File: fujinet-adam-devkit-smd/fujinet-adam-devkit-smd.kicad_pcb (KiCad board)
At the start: 2 copper layers, 57.8 x 55.3 mm, 39 parts, among them J1 RJ12, J2 RJ12, J3 SD_Card, Q1 MMBT3904, Q2 MMBT3906, SW1 ButtonA, SW2 ButtonB, SW3 Safe Reset, U1 ESP32-DEVKITC-32U

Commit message: Update docs
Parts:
- U1: value ESP32-DEVKITC-32U -> ESP32-DevKitC-VE

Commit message: Update SMD PCB and Case to v1.1, fix ADAMNet Out port not working
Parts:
- J1: value RJ12 -> In
- J2: value RJ12 -> Out
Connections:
- J2 pad 1: /ADAMNET_DATA -> /ADAMNET_5V
- J2 pad 2: /ADAMNET_RESET -> GND
- J2 pad 5: GND -> /ADAMNET_RESET
- J2 pad 6: /ADAMNET_5V -> /ADAMNET_DATA
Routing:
- net /ADAMNET_5V: track 58.3 -> 68.9 mm
- net /ADAMNET_DATA: track 51.6 -> 45.3 mm
- net /IO13/LED3/TCK: track 31.4 -> 32.2 mm
- net GND: vias 20 -> 18
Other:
- board text added: "v1.1"
- board text removed: "v1.0"
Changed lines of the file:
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@@
   (title_block
     (title "FujiNet ADAM Devkit SMD")
-    (date "2023-11-11")
-    (rev "1.0")
+    (date "2023-12-25")
+    (rev "1.1")
     (company "Chris Tersteeg")
   )
@@
         (effects (font (size 1 1) (thickness 0.15)))
     )
-    (fp_text value "RJ12" (at 3.54 18.3) (layer "F.Fab")
-        (effects (font (size 1 1) (thickness 0.15)))
+    (fp_text value "In" (at 3.54 13.081) (layer "B.SilkS")
+        (effects (font (size 1 1) (thickness 0.15)) (justify mirror))
     )
     (fp_text user "${REFERENCE}" (at 3.16 7.76) (layer "F.Fab")
@@
         (effects (font (size 1 1) (thickness 0.15)))
     )
-    (fp_text value "RJ12" (at 3.54 18.3) (layer "F.Fab")
-        (effects (font (size 1 1) (thickness 0.15)))
+    (fp_text value "Out" (at 3.424 13.081) (layer "B.SilkS")
+        (effects (font (size 1 1) (thickness 0.15)) (justify mirror))
     )
     (fp_text user "${REFERENCE}" (at 3.16 7.76) (layer "F.Fab")
@@
     (pad "" np_thru_hole circle (at 8.25 8.89) (size 3.25 3.25) (drill 3.25) (layers "*.Cu" "*.Mask"))
     (pad "1" thru_hole rect (at 0 0) (size 1.52 1.52) (drill 0.76) (layers "*.Cu" "*.Mask")
-      (net 10 "/ADAMNET_DATA") (pintype "passive"))
+      (net 6 "/ADAMNET_5V") (pintype "passive"))
     (pad "2" thru_hole circle (at 1.27 2.54) (size 1.52 1.52) (drill 0.76) (layers "*.Cu" "*.Mask")
-      (net 9 "/ADAMNET_RESET") (pintype "passive"))
+      (net 8 "GND") (pintype "passive"))
     (pad "3" thru_hole circle (at 2.54 0) (size 1.52 1.52) (drill 0.76) (layers "*.Cu" "*.Mask")
       (net 8 "GND") (pintype "passive"))
@@
       (net 8 "GND") (pintype "passive"))
     (pad "5" thru_hole circle (at 5.08 0) (size 1.52 1.52) (drill 0.76) (layers "*.Cu" "*.Mask")
-      (net 8 "GND") (pintype "passive"))
+      (net 9 "/ADAMNET_RESET") (pintype "passive"))
     (pad "6" thru_hole circle (at 6.35 2.54) (size 1.52 1.52) (drill 0.76) (layers "*.Cu" "*.Mask")
-      (net 6 "/ADAMNET_5V") (pintype "passive"))
+      (net 10 "/ADAMNET_DATA") (pintype "passive"))
     (model "C:/Users/cdter/Documents/Kicad/AMP-RJ12-54601-906WPLF.STEP"
       (offset (xyz 3.2 -16.8 0))
@@
     (effects (font (size 1 1) (thickness 0.15)) (justify left bottom))
   )
-  (gr_text "v1.0" (at 102.108 98.806 90) (layer "F.SilkS")
+  (gr_text "v1.1" (at 102.108 98.806 90) (layer "F.SilkS")
     (effects (font (size 1 1) (thickness 0.15)) (justify left bottom))
   )
@@
   (segment (start 134.715 130.175) (end 135.89 129) (width 0.7) (layer "F.Cu") (net 5))
   (segment (start 143.51 129) (end 143.478 129.032) (width 0.7) (layer "F.Cu") (net 5))
-  (segment (start 124.079 121.285) (end 112.527 121.285) (width 0.7) (layer "F.Cu") (net 6))
+  (segment (start 105.41 121.92) (end 123.444 121.92) (width 0.5) (layer "F.Cu") (net 6))
   (segment (start 128.315827 118.745) (end 133.96 118.745) (width 0.5) (layer "F.Cu") (net 6))
   (segment (start 138.43 114.665) (end 139.335 114.665) (width 0.25) (layer "F.Cu") (net 6))
   (segment (start 135.23 117.865) (end 138.43 114.665) (width 0.25) (layer "F.Cu") (net 6))
   (segment (start 125.73 119.634) (end 126.61 118.754) (width 0.5) (layer "F.Cu") (net 6))
+  (segment (start 104.14 120.65) (end 105.41 121.92) (width 0.5) (layer "F.Cu") (net 6))
   (segment (start 135.23 120.015) (end 135.23 124.34) (width 0.7) (layer "F.Cu") (net 6))
   (segment (start 128.306827 118.754) (end 128.315827 118.745) (width 0.5) (layer "F.Cu") (net 6))
   (segment (start 133.96 118.745) (end 135.23 120.015) (width 0.5) (layer "F.Cu") (net 6))
   (segment (start 135.23 124.34) (end 135.89 125) (width 0.7) (layer "F.Cu") (net 6))
-  (segment (start 112.527 121.285) (end 110.876 119.634) (width 0.7) (layer "F.Cu") (net 6))
+  (segment (start 123.444 121.92) (end 125.73 119.634) (width 0.5) (layer "F.Cu") (net 6))
+  (segment (start 104.14 117.48) (end 104.14 120.65) (width 0.5) (layer "F.Cu") (net 6))
   (segment (start 135.23 120.015) (end 135.23 117.865) (width 0.25) (layer "F.Cu") (net 6))
   (segment (start 143.51 98.425) (end 142.605 98.425) (width 0.25) (layer "F.Cu") (net 6))
+  (segment (start 104.526 117.094) (end 104.14 117.48) (width 0.5) (layer "F.Cu") (net 6))
   (segment (start 126.61 118.754) (end 128.306827 118.754) (width 0.5) (layer "F.Cu") (net 6))
-  (segment (start 125.73 119.634) (end 124.079 121.285) (width 0.7) (layer "F.Cu") (net 6))
   (segment (start 139.335 114.665) (end 139.7 114.3) (width 0.25) (layer "F.Cu") (net 6))
   (via (at 139.7 114.3) (size 0.6) (drill 0.3) (layers "F.Cu" "B.Cu") (net 6))
@@
   (segment (start 123.571 106.045) (end 124.265 106.045) (width 0.25) (layer "F.Cu") (net 8))
   (via (at 149.479 106.934) (size 0.8) (drill 0.4) (layers "F.Cu" "B.Cu") (free) (net 8))
-  (via (at 115.062 117.094) (size 0.8) (drill 0.4) (layers "F.Cu" "B.Cu") (free) (net 8))
   (via (at 136.906 103.505) (size 1) (drill 0.5) (layers "F.Cu" "B.Cu") (net 8))
   (via (at 146.05 90.678) (size 0.8) (drill 0.4) (layers "F.Cu" "B.Cu") (free) (net 8))
@@
   (via (at 128.778 102.997) (size 0.8) (drill 0.4) (layers "F.Cu" "B.Cu") (free) (net 8))
   (via (at 119.888 112.395) (size 0.8) (drill 0.4) (layers "F.Cu" "B.Cu") (free) (net 8))
-  (via (at 115.189 119.888) (size 0.8) (drill 0.4) (layers "F.Cu" "B.Cu") (free) (net 8))
   (via (at 112.014 108.331) (size 0.8) (drill 0.4) (layers "F.Cu" "B.Cu") (free) (net 8))
   (via (at 142.621 94.234) (size 1) (drill 0.5) (layers "F.Cu" "B.Cu") (free) (net 8))
@@
   (via (at 149.479 109.855) (size 0.8) (drill 0.4) (layers "F.Cu" "B.Cu") (free) (net 8))
   (segment (start 125.476 118.364) (end 121.92 118.364) (width 0.25) (layer "F.Cu") (net 9))
-  (segment (start 119.38 118.364) (end 107.066 118.364) (width 0.25) (layer "F.Cu") (net 9))
+  (segment (start 118.999 121.285) (end 120.65 119.634) (width 0.25) (layer "F.Cu") (net 9))
+  (segment (start 109.606 117.094) (end 109.606 120.467211) (width 0.25) (layer "F.Cu") (net 9))
   (segment (start 127.254 116.586) (end 125.476 118.364) (width 0.25) (layer "F.Cu") (net 9))
-  (segment (start 120.65 119.634) (end 119.38 118.364) (width 0.25) (layer "F.Cu") (net 9))
+  (segment (start 110.423789 121.285) (end 118.999 121.285) (width 0.25) (layer "F.Cu") (net 9))
   (segment (start 135.62 114.935) (end 133.339692 114.935) (width 0.25) (layer "F.Cu") (net 9))
   (segment (start 128.905 116.205) (end 128.524 116.586) (width 0.25) (layer "F.Cu") (net 9))
@@
   (segment (start 128.524 116.586) (end 127.254 116.586) (width 0.25) (layer "F.Cu") (net 9))
   (segment (start 133.339692 114.935) (end 132.069692 116.205) (width 0.25) (layer "F.Cu") (net 9))
+  (segment (start 109.606 120.467211) (end 110.423789 121.285) (width 0.25) (layer "F.Cu") (net 9))
   (segment (start 121.92 118.364) (end 120.65 119.634) (width 0.25) (layer "F.Cu") (net 9))
-  (segment (start 107.066 118.364) (end 105.796 119.634) (width 0.25) (layer "F.Cu") (net 9))
   (segment (start 132.069692 116.205) (end 128.905 116.205) (width 0.25) (layer "F.Cu") (net 9))
   (segment (start 128.201154 115.824) (end 120.65 115.824) (width 0.25) (layer "F.Cu") (net 10))
   (segment (start 120.65 115.824) (end 119.38 117.094) (width 0.25) (layer "F.Cu") (net 10))
-  (segment (start 104.526 117.094) (end 105.796 115.824) (width 0.25) (layer "F.Cu") (net 10))
   (segment (start 134.89 102.235) (end 135.915 101.21) (width 0.25) (layer "F.Cu") (net 10))
-  (segment (start 105.796 115.824) (end 118.11 115.824) (width 0.25) (layer "F.Cu") (net 10))
   (segment (start 130.360154 113.665) (end 128.201154 115.824) (width 0.25) (layer "F.Cu") (net 10))
+  (segment (start 116.84 119.634) (end 119.38 117.094) (width 0.25) (layer "F.Cu") (net 10))
   (segment (start 137.675 101.21) (end 138.7 102.235) (width 0.25) (layer "F.Cu") (net 10))
   (segment (start 133.35 113.665) (end 130.360154 113.665) (width 0.25) (layer "F.Cu") (net 10))
-  (segment (start 118.11 115.824) (end 119.38 117.094) (width 0.25) (layer "F.Cu") (net 10))
   (segment (start 135.915 101.21) (end 137.675 101.21) (width 0.25) (layer "F.Cu") (net 10))
+  (segment (start 110.876 119.634) (end 116.84 119.634) (width 0.25) (layer "F.Cu") (net 10))
   (segment (start 131.445 102.235) (end 133.35 102.235) (width 0.25) (layer "F.Cu") (net 10))
   (segment (start 133.35 102.235) (end 134.89 102.235) (width 0.25) (layer "F.Cu") (net 10))
@@
   (segment (start 123.42 110.53) (end 130.215 110.53) (width 0.25) (layer "F.Cu") (net 22))
   (segment (start 152.4 111.125) (end 153.035 111.76) (width 0.25) (layer "F.Cu") (net 22))
-  (segment (start 128.778 122.682) (end 131.445 120.015) (width 0.25) (layer "F.Cu") (net 23))
-  (segment (start 112.395 122.555) (end 112.522 122.682) (width 0.25) (layer "F.Cu") (net 23))
+  (segment (start 112.395 123.19) (end 128.27 123.19) (width 0.25) (layer "F.Cu") (net 23))
   (segment (start 112.395 111.395) (end 112.395 112.2955) (width 0.25) (layer "F.Cu") (net 23))
-  (segment (start 112.522 122.682) (end 128.778 122.682) (width 0.25) (layer "F.Cu") (net 23))
-  (via (at 112.395 122.555) (size 0.6) (drill 0.3) (layers "F.Cu" "B.Cu") (net 23))
+  (segment (start 128.27 123.19) (end 131.445 120.015) (width 0.25) (layer "F.Cu") (net 23))
+  (via (at 112.395 123.19) (size 0.6) (drill 0.3) (layers "F.Cu" "B.Cu") (net 23))
   (via (at 112.395 112.2955) (size 0.6) (drill 0.3) (layers "F.Cu" "B.Cu") (net 23))
-  (segment (start 112.395 112.2955) (end 112.395 122.555) (width 0.25) (layer "B.Cu") (net 23))
+  (segment (start 112.395 112.2955) (end 112.395 123.19) (width 0.25) (layer "B.Cu") (net 23))
   (segment (start 129.565154 109.38) (end 130.360154 108.585) (width 0.25) (layer "F.Cu") (net 24))
   (segment (start 103.615 109.38) (end 129.565154 109.38) (width 0.25) (layer "F.Cu") (net 24))

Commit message: v1.1 PCB tweak
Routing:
- net GND: vias 18 -> 27
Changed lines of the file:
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@@
   (segment (start 123.571 106.045) (end 124.265 106.045) (width 0.25) (layer "F.Cu") (net 8))
   (via (at 149.479 106.934) (size 0.8) (drill 0.4) (layers "F.Cu" "B.Cu") (free) (net 8))
+  (via (at 127.635 130.81) (size 0.8) (drill 0.4) (layers "F.Cu" "B.Cu") (free) (net 8))
   (via (at 136.906 103.505) (size 1) (drill 0.5) (layers "F.Cu" "B.Cu") (net 8))
   (via (at 146.05 90.678) (size 0.8) (drill 0.4) (layers "F.Cu" "B.Cu") (free) (net 8))
@@
   (via (at 120.777 101.346) (size 0.8) (drill 0.4) (layers "F.Cu" "B.Cu") (free) (net 8))
   (via (at 102.616 106.045) (size 0.6) (drill 0.3) (layers "F.Cu" "B.Cu") (free) (net 8))
+  (via (at 113.03 130.81) (size 0.8) (drill 0.4) (layers "F.Cu" "B.Cu") (free) (net 8))
   (via (at 146.05 88.138) (size 0.8) (drill 0.4) (layers "F.Cu" "B.Cu") (free) (net 8))
+  (via (at 117.475 130.81) (size 0.8) (drill 0.4) (layers "F.Cu" "B.Cu") (free) (net 8))
+  (via (at 141.605 117.475) (size 0.8) (drill 0.4) (layers "F.Cu" "B.Cu") (free) (net 8))
+  (via (at 154.305 130.175) (size 0.8) (drill 0.4) (layers "F.Cu" "B.Cu") (free) (net 8))
   (via (at 127.381 91.186) (size 0.8) (drill 0.4) (layers "F.Cu" "B.Cu") (free) (net 8))
   (via (at 128.778 102.997) (size 0.8) (drill 0.4) (layers "F.Cu" "B.Cu") (free) (net 8))
   (via (at 119.888 112.395) (size 0.8) (drill 0.4) (layers "F.Cu" "B.Cu") (free) (net 8))
+  (via (at 102.235 130.81) (size 0.8) (drill 0.4) (layers "F.Cu" "B.Cu") (free) (net 8))
   (via (at 112.014 108.331) (size 0.8) (drill 0.4) (layers "F.Cu" "B.Cu") (free) (net 8))
+  (via (at 141.605 122.555) (size 0.8) (drill 0.4) (layers "F.Cu" "B.Cu") (free) (net 8))
   (via (at 142.621 94.234) (size 1) (drill 0.5) (layers "F.Cu" "B.Cu") (free) (net 8))
   (via (at 108.966 108.331) (size 0.8) (drill 0.4) (layers "F.Cu" "B.Cu") (free) (net 8))
   (via (at 152.781 98.044) (size 1) (drill 0.5) (layers "F.Cu" "B.Cu") (free) (net 8))
   (via (at 113.284 101.346) (size 0.8) (drill 0.4) (layers "F.Cu" "B.Cu") (free) (net 8))
+  (via (at 133.35 123.825) (size 0.8) (drill 0.4) (layers "F.Cu" "B.Cu") (free) (net 8))
+  (via (at 139.7 120.015) (size 0.8) (drill 0.4) (layers "F.Cu" "B.Cu") (free) (net 8))
   (via (at 149.479 109.855) (size 0.8) (drill 0.4) (layers "F.Cu" "B.Cu") (free) (net 8))
   (segment (start 125.476 118.364) (end 121.92 118.364) (width 0.25) (layer "F.Cu") (net 9))
@@
   (segment (start 123.42 110.53) (end 130.215 110.53) (width 0.25) (layer "F.Cu") (net 22))
   (segment (start 152.4 111.125) (end 153.035 111.76) (width 0.25) (layer "F.Cu") (net 22))
+  (segment (start 128.27 123.19) (end 131.445 120.015) (width 0.25) (layer "F.Cu") (net 23))
   (segment (start 112.395 123.19) (end 128.27 123.19) (width 0.25) (layer "F.Cu") (net 23))
   (segment (start 112.395 111.395) (end 112.395 112.2955) (width 0.25) (layer "F.Cu") (net 23))
-  (segment (start 128.27 123.19) (end 131.445 120.015) (width 0.25) (layer "F.Cu") (net 23))
   (via (at 112.395 123.19) (size 0.6) (drill 0.3) (layers "F.Cu" "B.Cu") (net 23))
   (via (at 112.395 112.2955) (size 0.6) (drill 0.3) (layers "F.Cu" "B.Cu") (net 23))

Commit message: Add SMD version 1.2 PCB/case files and embossed text STL's for AMS printing
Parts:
- added JP1: Always On, Jumper:SolderJumper-2_P1.3mm_Open_RoundedPad1.0x1.5mm, F.Cu at (140.7, 125.6)
- added S1: SK12D07VG4, SK12D07VG4:SK12D07VG4, F.Cu at (144.1, 130.2)
- moved D5 9.65 mm to (153.2, 127.0)
- moved D4 0.76 mm to (135.1, 127.0)
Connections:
- D4 pad 2: /ADAMNET_5V -> Net-(D4-A)
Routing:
- net +5V: track 12.5 -> 24.4 mm
- net Net-(D4-A): track 0.00 -> 10.6 mm
- net /ADAMNET_5V: track 68.9 -> 78.2 mm
- net Net-(D5-K): track 26.5 -> 28.1 mm
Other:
- board text added: "v1.2"
- board text removed: "v1.1"

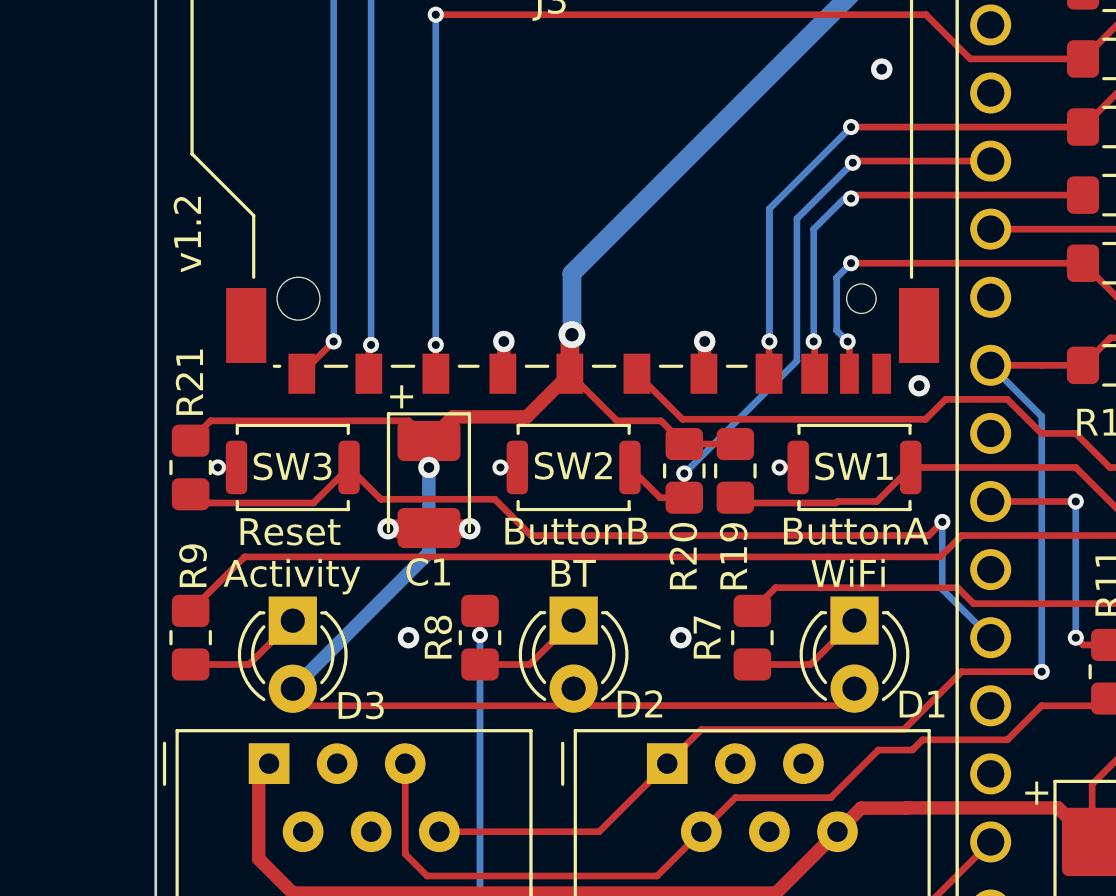
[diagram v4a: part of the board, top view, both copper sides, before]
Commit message: Update SMD version to 1.3 Add tall case for versions with a power switch
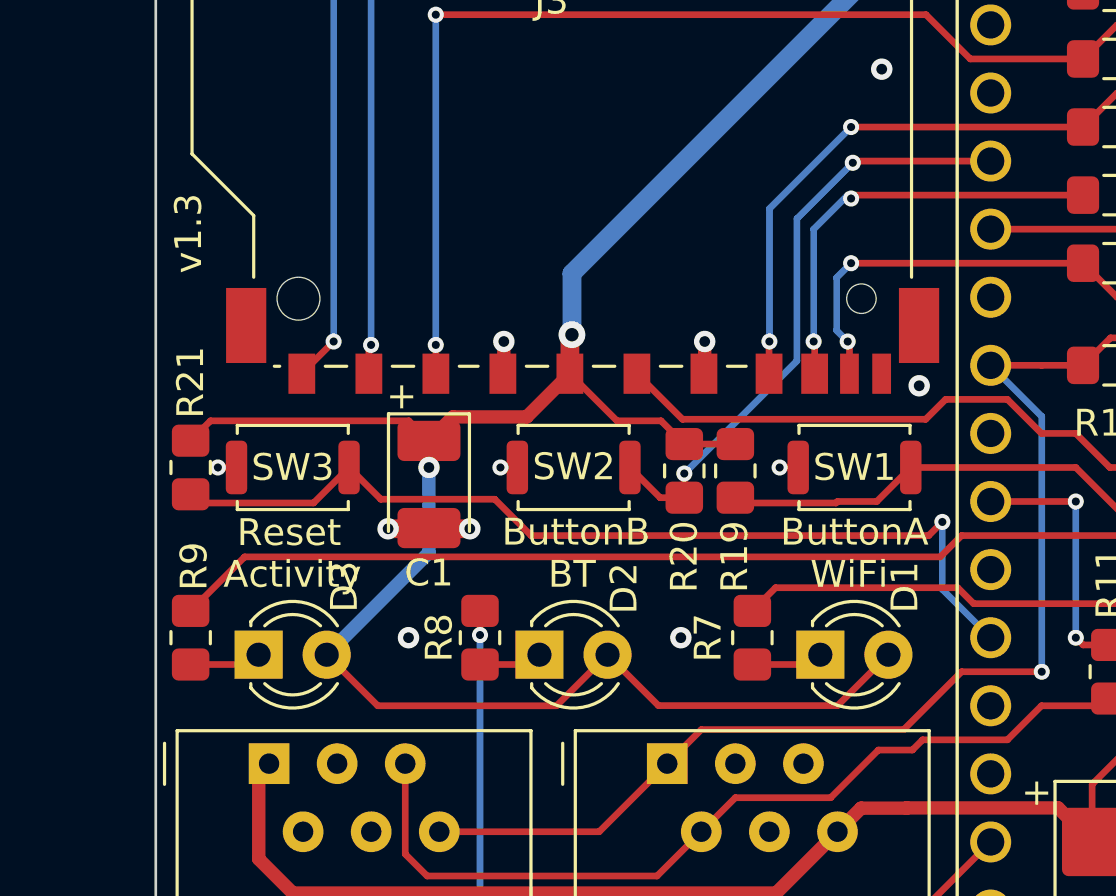
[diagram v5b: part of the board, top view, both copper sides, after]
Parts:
- moved D2 1.80 mm to (114.6, 113.0), turned to 0 degrees
- moved D1 1.80 mm to (125.1, 113.0), turned to 0 degrees
- moved D3 1.80 mm to (104.1, 113.0), turned to 0 degrees
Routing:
- net Net-(D2-K): track 4.17 -> 2.37 mm
- net Net-(D1-K): track 4.49 -> 2.69 mm
- net Net-(D3-K): track 4.49 -> 2.69 mm
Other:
- board text added: "v1.3"
- board text removed: "v1.2"
